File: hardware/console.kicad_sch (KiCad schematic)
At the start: 54 parts, among them J1 USB-C_Module, J3 SWD, J4 UART, J5 LiPo_140mAh, SW1 SW_LEFT, SW10 SW_BOOT0, SW2 SW_RIGHT, SW3 SW_UP, SW4 SW_DOWN, SW5 SW_A, SW6 SW_B, SW7 SW_POWER, SW8 SW_START, SW9 SW_SELECT, U1 STM32G0B1CBT6, U2 XC6206P332MR, U3 TP4054

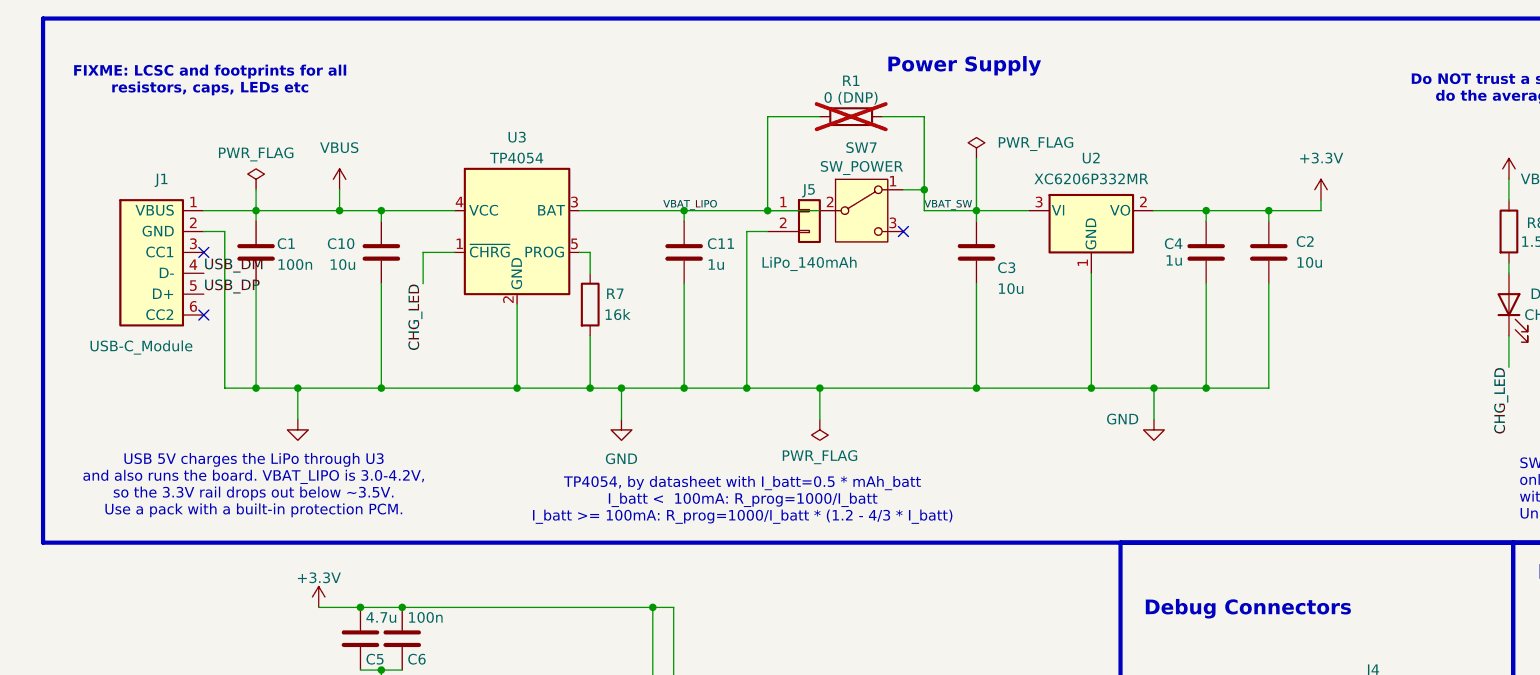
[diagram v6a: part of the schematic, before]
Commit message: resistor and caps footprints
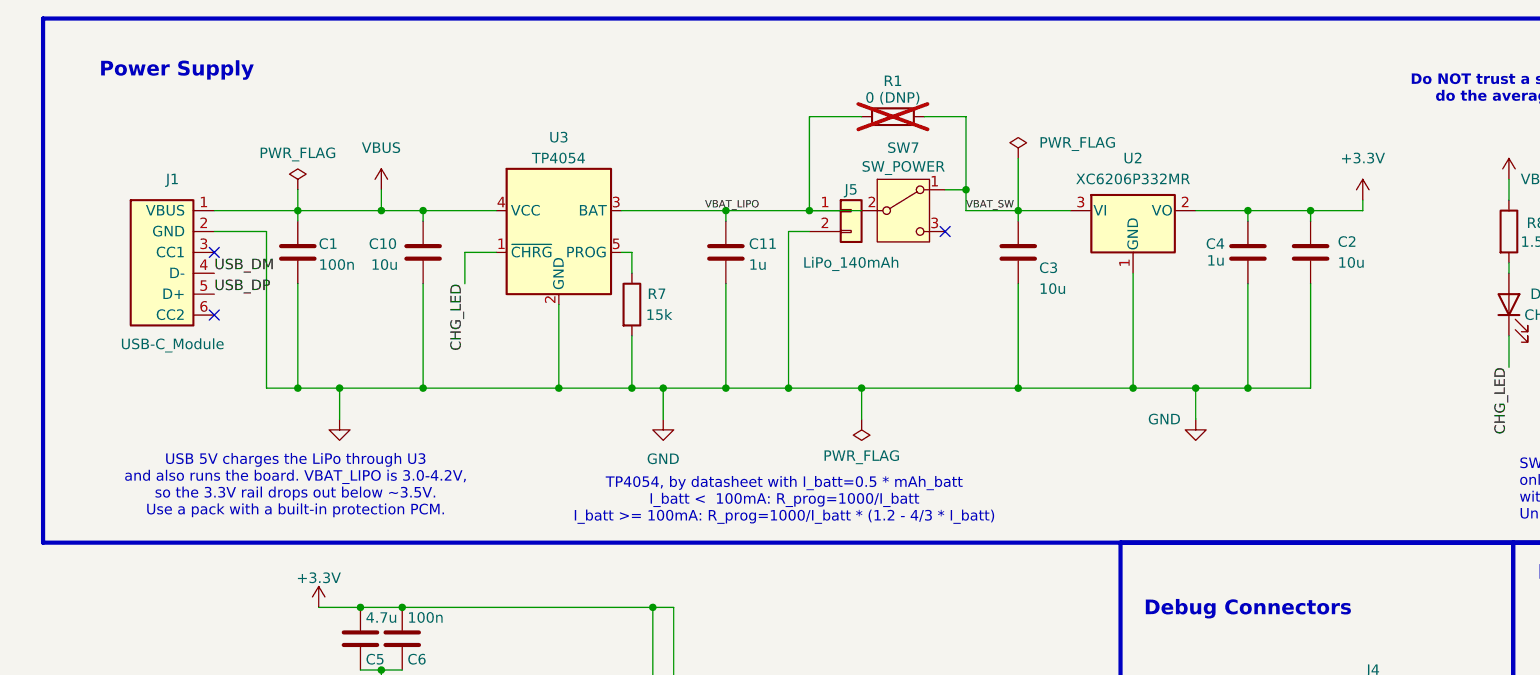
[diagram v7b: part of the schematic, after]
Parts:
- C1, C12, C6, C8, C9: Dielectric (none) -> X7R; LCSC (none) -> C1525; MPN (none) -> CL05B104KO5NNNC; Voltage (none) -> 16V
- C10, C2, C3: Dielectric (none) -> X5R; LCSC (none) -> C15850; MPN (none) -> CL21A106KAYNNNE; Voltage (none) -> 25V
- C11, C4, C7: Dielectric (none) -> X5R; LCSC (none) -> C52923; MPN (none) -> CL05A105KA5NQNC; Voltage (none) -> 25V
- C5: Dielectric (none) -> X5R; LCSC (none) -> C19666; MPN (none) -> CL10A475KO8NNNC; Voltage (none) -> 16V
- D1: LCSC (none) -> C2286; MPN (none) -> KT-0603R; Manufacturer (none) -> Hubei KENTO Elec
- R10, R9: footprint Resistor_SMD:R_0402_1005Metric -> Resistor_SMD:R_0603_1608Metric; LCSC (none) -> C23178; MPN (none) -> 0603WAF4703T5E
- R11: LCSC (none) -> C25744; MPN (none) -> 0402WGF1002TCE; Tolerance (none) -> 1%
- R4, R5: LCSC (none) -> C25900; MPN (none) -> 0402WGF4701TCE; Tolerance (none) -> 1%
- R6: LCSC (none) -> C25076; MPN (none) -> 0402WGF1000TCE; Tolerance (none) -> 1%
- R7: value 16k -> 15k; LCSC (none) -> C25756; MPN (none) -> 0402WGF1502TCE
- R8: LCSC (none) -> C25867; MPN (none) -> 0402WGF1501TCE; Tolerance (none) -> 1%
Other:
- note removed: "FIXME: LCSC and footprints for all resistors, caps, LEDs etc"
- moved on the sheet: C1, C10, C11, C2, C3, C4, J1, J5, R1, R7, SW7, U2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

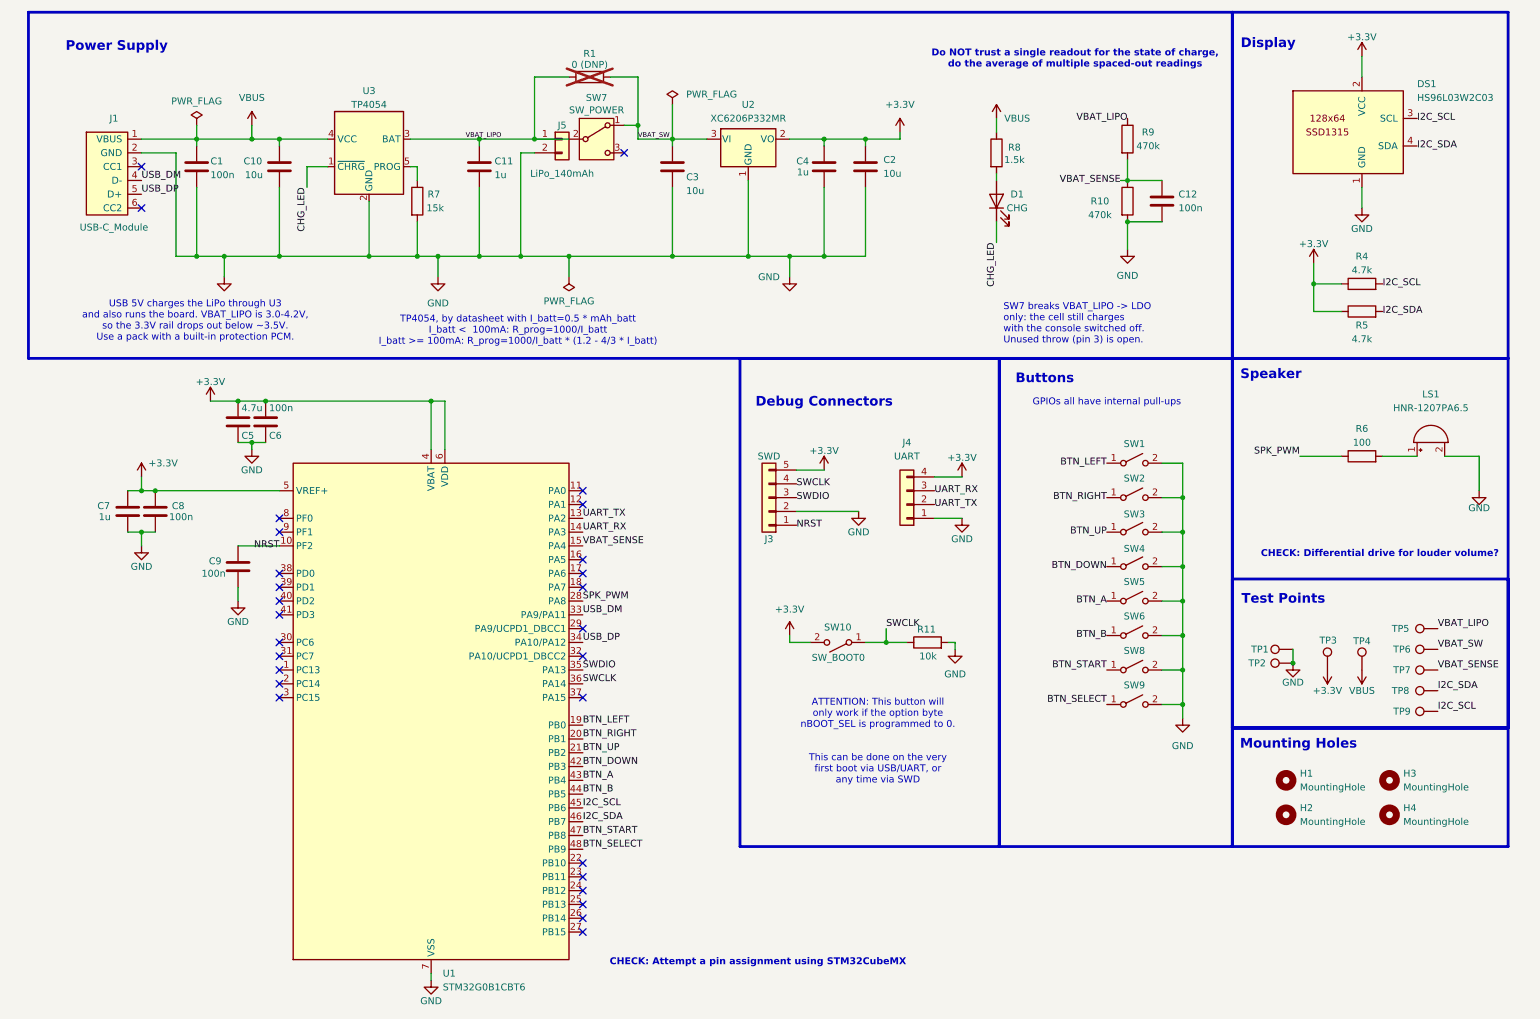
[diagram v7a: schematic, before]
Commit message: validated pinout + stm32cubemx .ioc
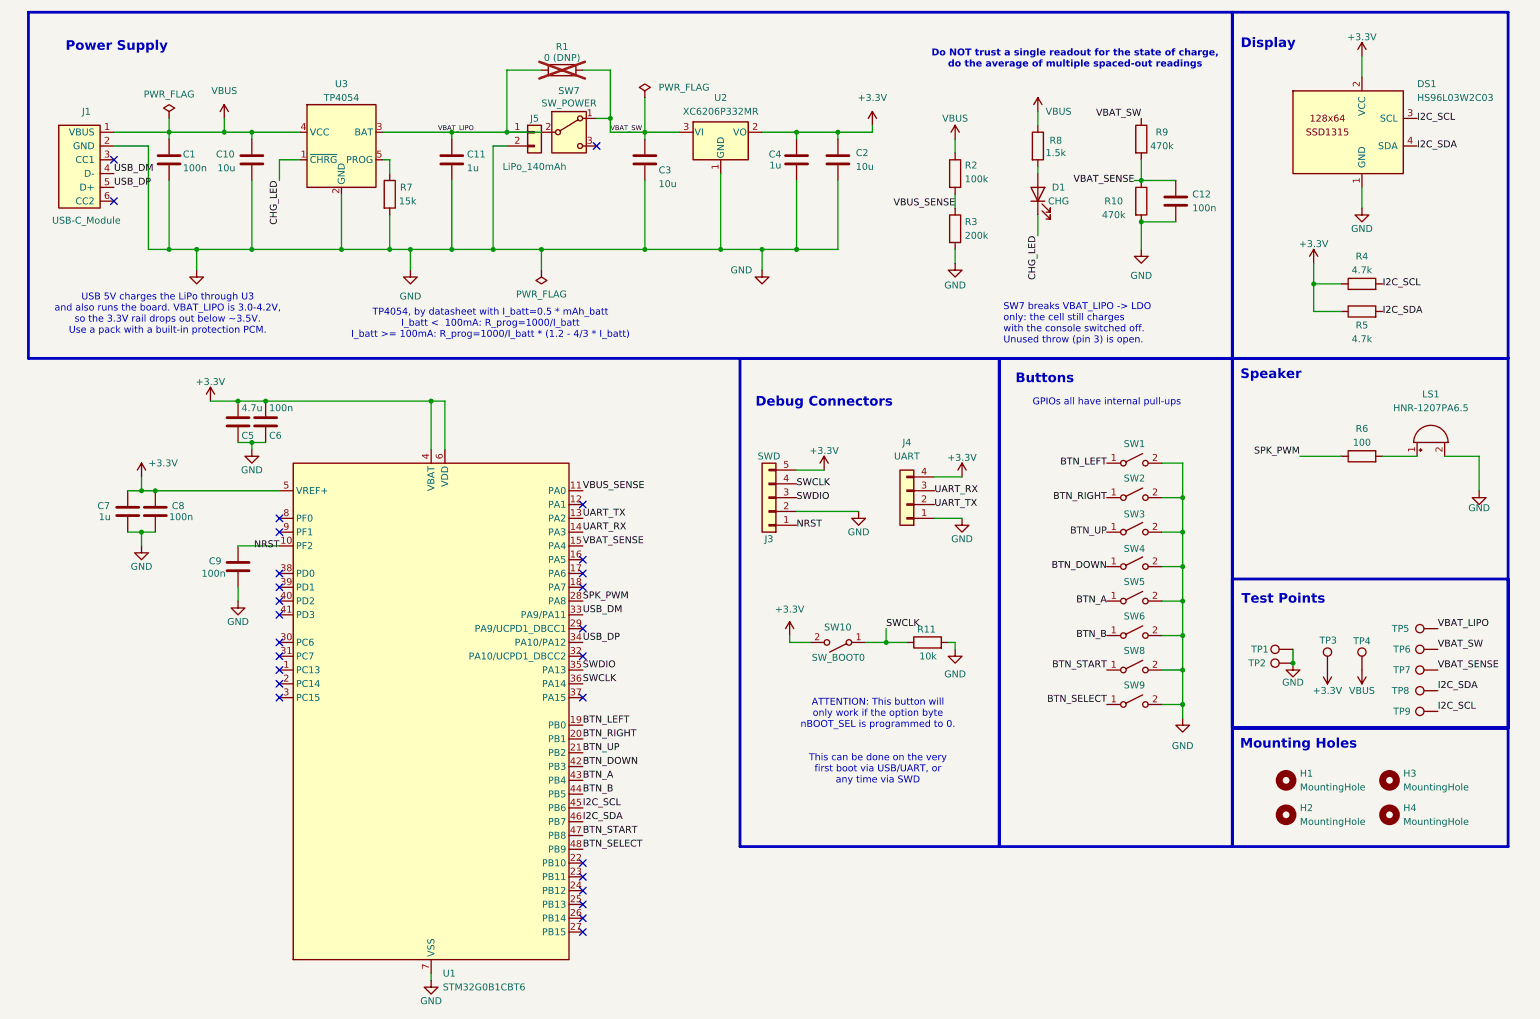
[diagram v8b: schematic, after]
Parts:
- added R2: 100k, Resistor_SMD:R_0402_1005Metric, symbol Device:R
- added R3: 200k, Resistor_SMD:R_0402_1005Metric, symbol Device:R
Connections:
- net GND: now also R3.2
- net VBAT_LIPO: no longer R9.1
- net VBAT_SW: now also R9.1
- net VBUS: now also R2.1
- net VBUS_SENSE: now reaches U1.11 (PA0)
- net VBUS_SENSE: now also R2.2, R3.1
- no-connect marks 28 -> 27
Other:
- note removed: "CHECK: Attempt a pin assignment using STM32CubeMX"
- note removed: "CHECK: Differential drive for louder volume?"
- moved on the sheet: C1, C10, C11, C12, C2, C3, C4, D1, J1, J5, R1, R10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
